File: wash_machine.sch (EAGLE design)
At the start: 35 parts, among them IC1 7805TV, Q1 16MHz, U1 ATMEGA328P-PU

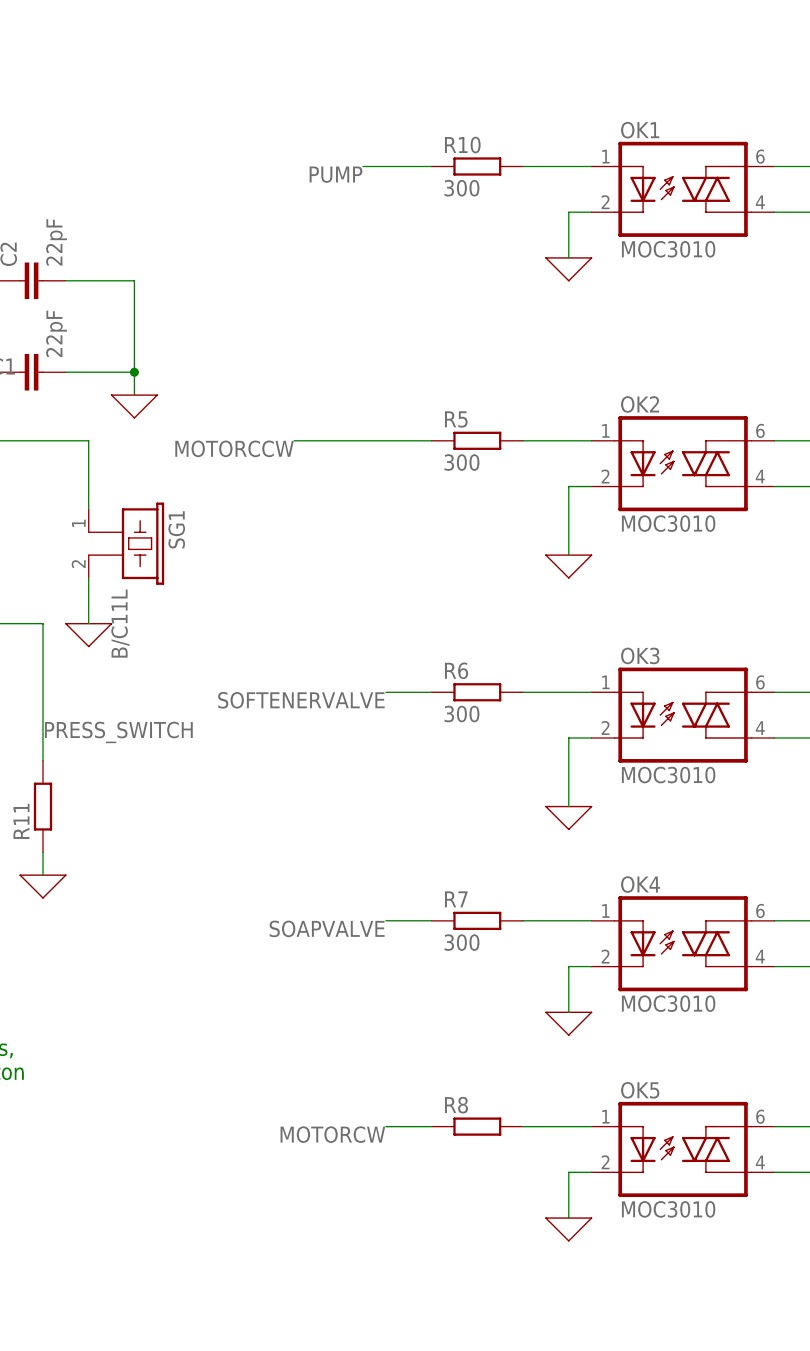
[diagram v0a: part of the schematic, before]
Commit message: Add debug leds
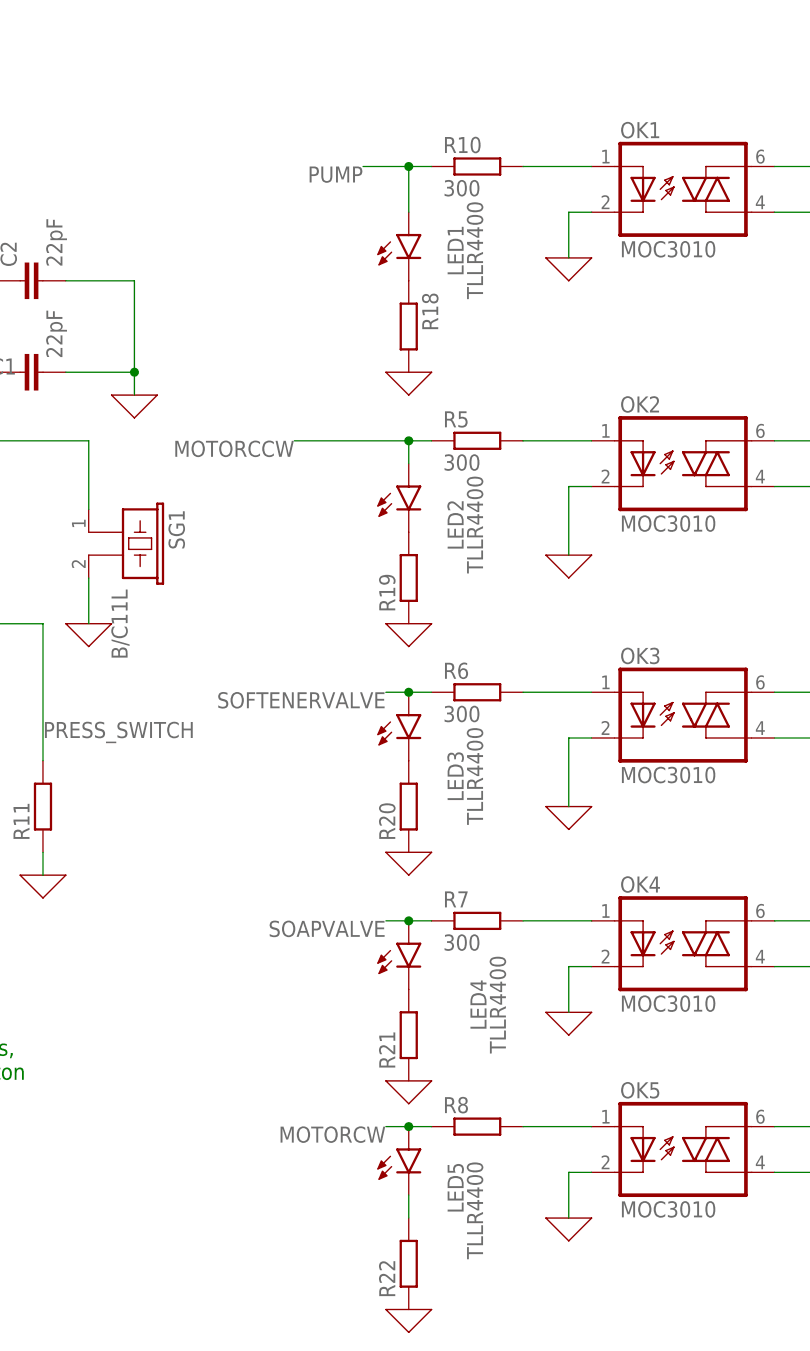
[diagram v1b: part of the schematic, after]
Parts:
- added LED1, LED2, LED3, LED4, LED5: TLLR4400, led:TLLR4400
- added R18, R19, R20, R21, R22: (no value), rcl:R-EU_0204/7
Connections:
- new net N$28: LED1.C, R18.1
- new net N$29: LED2.C, R19.2
- new net N$30: LED3.C, R20.2
- new net N$31: LED4.C, R21.2
- new net N$32: LED5.C, R22.2
- net 0: now also R18.2, R19.1, R20.1, R21.1, R22.1
- net MOTORCCW: now also LED2.A
- net MOTORCW: now also LED5.A
- net PUMP: now also LED1.A
- net SOAPVALVE: now also LED4.A
- net SOFTENERVALVE: now also LED3.A
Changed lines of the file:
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@@
 <part name="X5" library="con-molex" library_urn="urn:adsk.eagle:library:165" deviceset="KK-156-12" device="" package3d_urn="urn:adsk.eagle:package:8078817/1"/>
 <part name="X1" library="con-molex" library_urn="urn:adsk.eagle:library:165" deviceset="KK-156-12" device="" package3d_urn="urn:adsk.eagle:package:8078817/1"/>
+<part name="R18" library="rcl" library_urn="urn:adsk.eagle:library:334" deviceset="R-EU_" device="0204/7" package3d_urn="urn:adsk.eagle:package:23498/2"/>
+<part name="R19" library="rcl" library_urn="urn:adsk.eagle:library:334" deviceset="R-EU_" device="0204/7" package3d_urn="urn:adsk.eagle:package:23498/2"/>
+<part name="R20" library="rcl" library_urn="urn:adsk.eagle:library:334" deviceset="R-EU_" device="0204/7" package3d_urn="urn:adsk.eagle:package:23498/2"/>
+<part name="R21" library="rcl" library_urn="urn:adsk.eagle:library:334" deviceset="R-EU_" device="0204/7" package3d_urn="urn:adsk.eagle:package:23498/2"/>
+<part name="R22" library="rcl" library_urn="urn:adsk.eagle:library:334" deviceset="R-EU_" device="0204/7" package3d_urn="urn:adsk.eagle:package:23498/2"/>
+<part name="LED1" library="led" library_urn="urn:adsk.eagle:library:259" deviceset="TLLR4400" device="" package3d_urn="urn:adsk.eagle:package:15797/1"/>
+<part name="LED2" library="led" library_urn="urn:adsk.eagle:library:259" deviceset="TLLR4400" device="" package3d_urn="urn:adsk.eagle:package:15797/1"/>
+<part name="LED3" library="led" library_urn="urn:adsk.eagle:library:259" deviceset="TLLR4400" device="" package3d_urn="urn:adsk.eagle:package:15797/1"/>
+<part name="LED4" library="led" library_urn="urn:adsk.eagle:library:259" deviceset="TLLR4400" device="" package3d_urn="urn:adsk.eagle:package:15797/1"/>
+<part name="LED5" library="led" library_urn="urn:adsk.eagle:library:259" deviceset="TLLR4400" device="" package3d_urn="urn:adsk.eagle:package:15797/1"/>
+<part name="X_21" library="ngspice-simulation" library_urn="urn:adsk.eagle:library:527439" deviceset="GND" device=""/>
+<part name="X_22" library="ngspice-simulation" library_urn="urn:adsk.eagle:library:527439" deviceset="GND" device=""/>
+<part name="X_23" library="ngspice-simulation" library_urn="urn:adsk.eagle:library:527439" deviceset="GND" device=""/>
+<part name="X_24" library="ngspice-simulation" library_urn="urn:adsk.eagle:library:527439" deviceset="GND" device=""/>
+<part name="X_25" library="ngspice-simulation" library_urn="urn:adsk.eagle:library:527439" deviceset="GND" device=""/>
 </parts>
 <sheets>
@@
 <attribute name="NAME" x="116.84" y="59.182" size="1.524" layer="95" rot="MR180"/>
 </instance>
+<instance part="R18" gate="G$1" x="25.4" y="81.28" smashed="yes" rot="R270">
+<attribute name="NAME" x="26.8986" y="85.09" size="1.778" layer="95" rot="R270"/>
+<attribute name="VALUE" x="22.098" y="85.09" size="1.778" layer="96" rot="R270"/>
+</instance>
+<instance part="R19" gate="G$1" x="25.4" y="53.34" smashed="yes" rot="R90">
+<attribute name="NAME" x="23.9014" y="49.53" size="1.778" layer="95" rot="R90"/>
+<attribute name="VALUE" x="28.702" y="49.53" size="1.778" layer="96" rot="R90"/>
+</instance>
+<instance part="R20" gate="G$1" x="25.4" y="27.94" smashed="yes" rot="R90">
+<attribute name="NAME" x="23.9014" y="24.13" size="1.778" layer="95" rot="R90"/>
+<attribute name="VALUE" x="28.702" y="24.13" size="1.778" layer="96" rot="R90"/>
+</instance>
+<instance part="R21" gate="G$1" x="25.4" y="2.54" smashed="yes" rot="R90">
+<attribute name="NAME" x="23.9014" y="-1.27" size="1.778" layer="95" rot="R90"/>
+<attribute name="VALUE" x="28.702" y="-1.27" size="1.778" layer="96" rot="R90"/>
+</instance>
+<instance part="R22" gate="G$1" x="25.4" y="-22.86" smashed="yes" rot="R90">
+<attribute name="NAME" x="23.9014" y="-26.67" size="1.778" layer="95" rot="R90"/>
+<attribute name="VALUE" x="28.702" y="-26.67" size="1.778" layer="96" rot="R90"/>
+</instance>
+<instance part="LED1" gate="G$1" x="25.4" y="91.44" smashed="yes">
+<attribute name="NAME" x="31.496" y="86.868" size="1.778" layer="95" rot="R90"/>
+<attribute name="VALUE" x="33.655" y="84.328" size="1.778" layer="96" rot="R90"/>
+</instance>
+<instance part="LED2" gate="G$1" x="25.4" y="63.5" smashed="yes">
+<attribute name="NAME" x="31.496" y="56.388" size="1.778" layer="95" rot="R90"/>
+<attribute name="VALUE" x="33.655" y="53.848" size="1.778" layer="96" rot="R90"/>
+</instance>
+<instance part="LED3" gate="G$1" x="25.4" y="38.1" smashed="yes">
+<attribute name="NAME" x="31.496" y="28.448" size="1.778" layer="95" rot="R90"/>
+<attribute name="VALUE" x="33.655" y="25.908" size="1.778" layer="96" rot="R90"/>
+</instance>
+<instance part="LED4" gate="G$1" x="25.4" y="12.7" smashed="yes">
+<attribute name="NAME" x="34.036" y="3.048" size="1.778" layer="95" rot="R90"/>
+<attribute name="VALUE" x="36.195" y="0.508" size="1.778" layer="96" rot="R90"/>
+</instance>
+<instance part="LED5" gate="G$1" x="25.4" y="-10.16" smashed="yes">
+<attribute name="NAME" x="31.496" y="-17.272" size="1.778" layer="95" rot="R90"/>
+<attribute name="VALUE" x="33.655" y="-22.352" size="1.778" layer="96" rot="R90"/>
+</instance>
+<instance part="X_21" gate="G$1" x="25.4" y="48.26" smashed="yes"/>
+<instance part="X_22" gate="G$1" x="25.4" y="22.86" smashed="yes"/>
+<instance part="X_23" gate="G$1" x="25.4" y="-2.54" smashed="yes"/>
+<instance part="X_24" gate="G$1" x="25.4" y="-27.94" smashed="yes"/>
+<instance part="X_25" gate="G$1" x="25.4" y="76.2" smashed="yes"/>
 </instances>
 <busses>
@@
 <wire x1="5.08" y1="157.48" x2="5.08" y2="152.4" width="0.1524" layer="91"/>
 </segment>
+<segment>
+<pinref part="R19" gate="G$1" pin="1"/>
+<pinref part="X_21" gate="G$1" pin="0"/>
+</segment>
+<segment>
+<pinref part="X_22" gate="G$1" pin="0"/>
+<pinref part="R20" gate="G$1" pin="1"/>
+</segment>
+<segment>
+<pinref part="X_23" gate="G$1" pin="0"/>
+<pinref part="R21" gate="G$1" pin="1"/>
+</segment>
+<segment>
+<pinref part="X_24" gate="G$1" pin="0"/>
+<pinref part="R22" gate="G$1" pin="1"/>
+</segment>
+<segment>
+<pinref part="X_25" gate="G$1" pin="0"/>
+<pinref part="R18" gate="G$1" pin="2"/>
+</segment>
 </net>
 <net name="N$4" class="0">
@@
 <segment>
 <pinref part="R10" gate="G$1" pin="1"/>
-<wire x1="27.94" y1="99.06" x2="20.32" y2="99.06" width="0.1524" layer="91"/>
+<wire x1="27.94" y1="99.06" x2="25.4" y2="99.06" width="0.1524" layer="91"/>
 <label x="20.32" y="99.06" size="1.778" layer="95" rot="R180"/>
+<pinref part="LED1" gate="G$1" pin="A"/>
+<wire x1="25.4" y1="99.06" x2="20.32" y2="99.06" width="0.1524" layer="91"/>
+<wire x1="25.4" y1="93.98" x2="25.4" y2="99.06" width="0.1524" layer="91"/>
+<junction x="25.4" y="99.06"/>
 </segment>
 </net>
@@
 <pinref part="R5" gate="G$1" pin="1"/>
 <label x="12.7" y="68.58" size="1.778" layer="95" rot="R180"/>
-<wire x1="27.94" y1="68.58" x2="12.7" y2="68.58" width="0.1524" layer="91"/>
+<wire x1="27.94" y1="68.58" x2="25.4" y2="68.58" width="0.1524" layer="91"/>
+<pinref part="LED2" gate="G$1" pin="A"/>
+<wire x1="25.4" y1="68.58" x2="12.7" y2="68.58" width="0.1524" layer="91"/>
+<wire x1="25.4" y1="66.04" x2="25.4" y2="68.58" width="0.1524" layer="91"/>
+<junction x="25.4" y="68.58"/>
 </segment>
 </net>
@@
 <segment>
 <pinref part="R6" gate="G$1" pin="1"/>
-<wire x1="27.94" y1="40.64" x2="22.86" y2="40.64" width="0.1524" layer="91"/>
+<wire x1="27.94" y1="40.64" x2="25.4" y2="40.64" width="0.1524" layer="91"/>
 <label x="22.86" y="40.64" size="1.778" layer="95" rot="R180"/>
+<pinref part="LED3" gate="G$1" pin="A"/>
+<wire x1="25.4" y1="40.64" x2="22.86" y2="40.64" width="0.1524" layer="91"/>
+<junction x="25.4" y="40.64"/>
 </segment>
 </net>
@@
 <segment>
 <pinref part="R7" gate="G$1" pin="1"/>
-<wire x1="27.94" y1="15.24" x2="22.86" y2="15.24" width="0.1524" layer="91"/>
+<wire x1="27.94" y1="15.24" x2="25.4" y2="15.24" width="0.1524" layer="91"/>
 <label x="22.86" y="15.24" size="1.778" layer="95" rot="R180"/>
+<pinref part="LED4" gate="G$1" pin="A"/>
+<wire x1="25.4" y1="15.24" x2="22.86" y2="15.24" width="0.1524" layer="91"/>
+<junction x="25.4" y="15.24"/>
 </segment>
 </net>
@@
 <segment>
 <pinref part="R8" gate="G$1" pin="1"/>
-<wire x1="27.94" y1="-7.62" x2="22.86" y2="-7.62" width="0.1524" layer="91"/>
+<wire x1="27.94" y1="-7.62" x2="25.4" y2="-7.62" width="0.1524" layer="91"/>
 <label x="22.86" y="-7.62" size="1.778" layer="95" rot="R180"/>
+<pinref part="LED5" gate="G$1" pin="A"/>
+<wire x1="25.4" y1="-7.62" x2="22.86" y2="-7.62" width="0.1524" layer="91"/>
+<junction x="25.4" y="-7.62"/>
 </segment>
 </net>
@@
 </segment>
 </net>
+<net name="N$28" class="0">
+<segment>
+<pinref part="LED1" gate="G$1" pin="C"/>
+<pinref part="R18" gate="G$1" pin="1"/>
+</segment>
+</net>
+<net name="N$29" class="0">
+<segment>
+<pinref part="R19" gate="G$1" pin="2"/>
+<pinref part="LED2" gate="G$1" pin="C"/>
+</segment>
+</net>
+<net name="N$30" class="0">
+<segment>
+<pinref part="R20" gate="G$1" pin="2"/>
+<pinref part="LED3" gate="G$1" pin="C"/>
+</segment>
+</net>
+<net name="N$31" class="0">
+<segment>
+<pinref part="LED4" gate="G$1" pin="C"/>
+<pinref part="R21" gate="G$1" pin="2"/>
+</segment>
+</net>
+<net name="N$32" class="0">
+<segment>
+<pinref part="R22" gate="G$1" pin="2"/>
+<pinref part="LED5" gate="G$1" pin="C"/>
+<wire x1="25.4" y1="-17.78" x2="25.4" y2="-15.24" width="0.1524" layer="91"/>
+</segment>
+</net>

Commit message: Correct capacitors names
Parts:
- added C3: 10uF, rcl:CPOL-EUB45181A
- added C4: 100uF, rcl:CPOL-EUB45181A
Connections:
- net 0: now also C3.-, C4.-
- net N$2: now also C3.+
- net VCC: now also C4.+
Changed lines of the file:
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@@
 <part name="C1" library="capacitor-wima" library_urn="urn:adsk.eagle:library:116" deviceset="C" device="2,5-3" package3d_urn="urn:adsk.eagle:package:5436/1" value="22pF"/>
 <part name="C2" library="capacitor-wima" library_urn="urn:adsk.eagle:library:116" deviceset="C" device="2,5-3" package3d_urn="urn:adsk.eagle:package:5436/1" value="22pF"/>
-<part name="C3" library="docu-dummy" library_urn="urn:adsk.eagle:library:215" deviceset="ELKO" device="">
-<attribute name="C1" value="10uF"/>
-</part>
-<part name="C4" library="docu-dummy" library_urn="urn:adsk.eagle:library:215" deviceset="ELKO" device="">
-<attribute name="C2" value="100uF"/>
-</part>
 <part name="SG1" library="buzzer" library_urn="urn:adsk.eagle:library:113" deviceset="B/C11L" device="" package3d_urn="urn:adsk.eagle:package:5280/1"/>
 <part name="R1" library="rcl" library_urn="urn:adsk.eagle:library:334" deviceset="R-EU_" device="0204/7" package3d_urn="urn:adsk.eagle:package:23498/2"/>
@@
 <part name="X_24" library="ngspice-simulation" library_urn="urn:adsk.eagle:library:527439" deviceset="GND" device=""/>
 <part name="X_25" library="ngspice-simulation" library_urn="urn:adsk.eagle:library:527439" deviceset="GND" device=""/>
+<part name="C3" library="rcl" library_urn="urn:adsk.eagle:library:334" deviceset="CPOL-EU" device="B45181A" package3d_urn="urn:adsk.eagle:package:23316/1" value="10uF"/>
+<part name="C4" library="rcl" library_urn="urn:adsk.eagle:library:334" deviceset="CPOL-EU" device="B45181A" package3d_urn="urn:adsk.eagle:package:23316/1" value="100uF"/>
 </parts>
 <sheets>
@@
 <attribute name="VALUE" x="-13.081" y="87.884" size="1.778" layer="96" rot="R90"/>
 </instance>
-<instance part="C3" gate="G$1" x="-91.44" y="111.76" smashed="yes">
-<attribute name="C1" x="-91.44" y="111.76" size="1.778" layer="96" display="both"/>
-</instance>
-<instance part="C4" gate="G$1" x="-58.42" y="111.76" smashed="yes">
-<attribute name="C2" x="-58.42" y="111.76" size="1.778" layer="96" display="both"/>
-</instance>
 <instance part="SG1" gate="G$1" x="-7.62" y="58.42" smashed="yes" rot="R270">
 <attribute name="NAME" x="-1.27" y="60.96" size="1.778" layer="95" rot="R270"/>
@@
 <instance part="X_24" gate="G$1" x="25.4" y="-27.94" smashed="yes"/>
 <instance part="X_25" gate="G$1" x="25.4" y="76.2" smashed="yes"/>
+<instance part="C3" gate="G$1" x="-91.44" y="111.76" smashed="yes">
+<attribute name="NAME" x="-90.297" y="112.2426" size="1.778" layer="95"/>
+<attribute name="VALUE" x="-90.297" y="107.1626" size="1.778" layer="96"/>
+</instance>
+<instance part="C4" gate="G$1" x="-58.42" y="111.76" smashed="yes">
+<attribute name="NAME" x="-57.277" y="112.2426" size="1.778" layer="95"/>
+<attribute name="VALUE" x="-57.277" y="107.1626" size="1.778" layer="96"/>
+</instance>
 </instances>
 <busses>
@@
 <wire x1="-91.44" y1="114.3" x2="-91.44" y2="129.54" width="0.1524" layer="91"/>
 <junction x="-91.44" y="129.54"/>
+<pinref part="C3" gate="G$1" pin="+"/>
 </segment>
 </net>
@@
 <junction x="-58.42" y="129.54"/>
 <label x="-22.86" y="129.54" size="1.778" layer="95"/>
+<pinref part="C4" gate="G$1" pin="+"/>
 </segment>
 <segment>
@@
 <pinref part="X_1" gate="G$1" pin="0"/>
 <wire x1="-76.2" y1="101.6" x2="-76.2" y2="96.52" width="0.1524" layer="91"/>
-</segment>
-<segment>
+<pinref part="C3" gate="G$1" pin="-"/>
+<pinref part="C4" gate="G$1" pin="-"/>
+</segment>
+<segment>

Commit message: Rename ground signal from 0 to GND
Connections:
- net 0 renamed GND
